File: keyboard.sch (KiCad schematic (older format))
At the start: 180 parts, among them SW1 SW_Push, U1 ATmega32U4-AU, Y1 16MHz

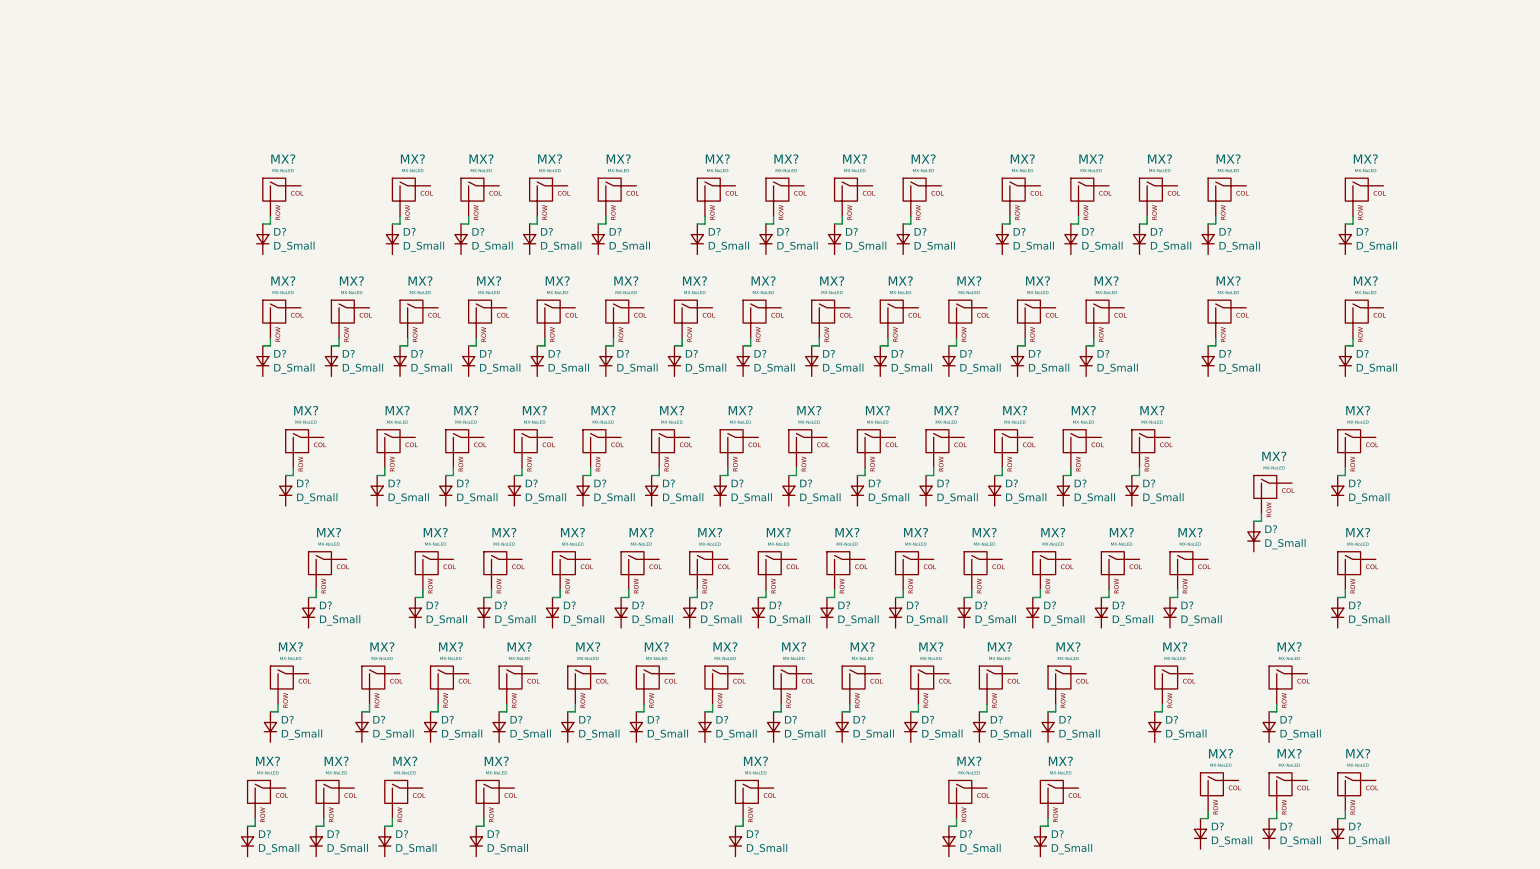
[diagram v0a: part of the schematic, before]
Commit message: Added labels for rows and columns
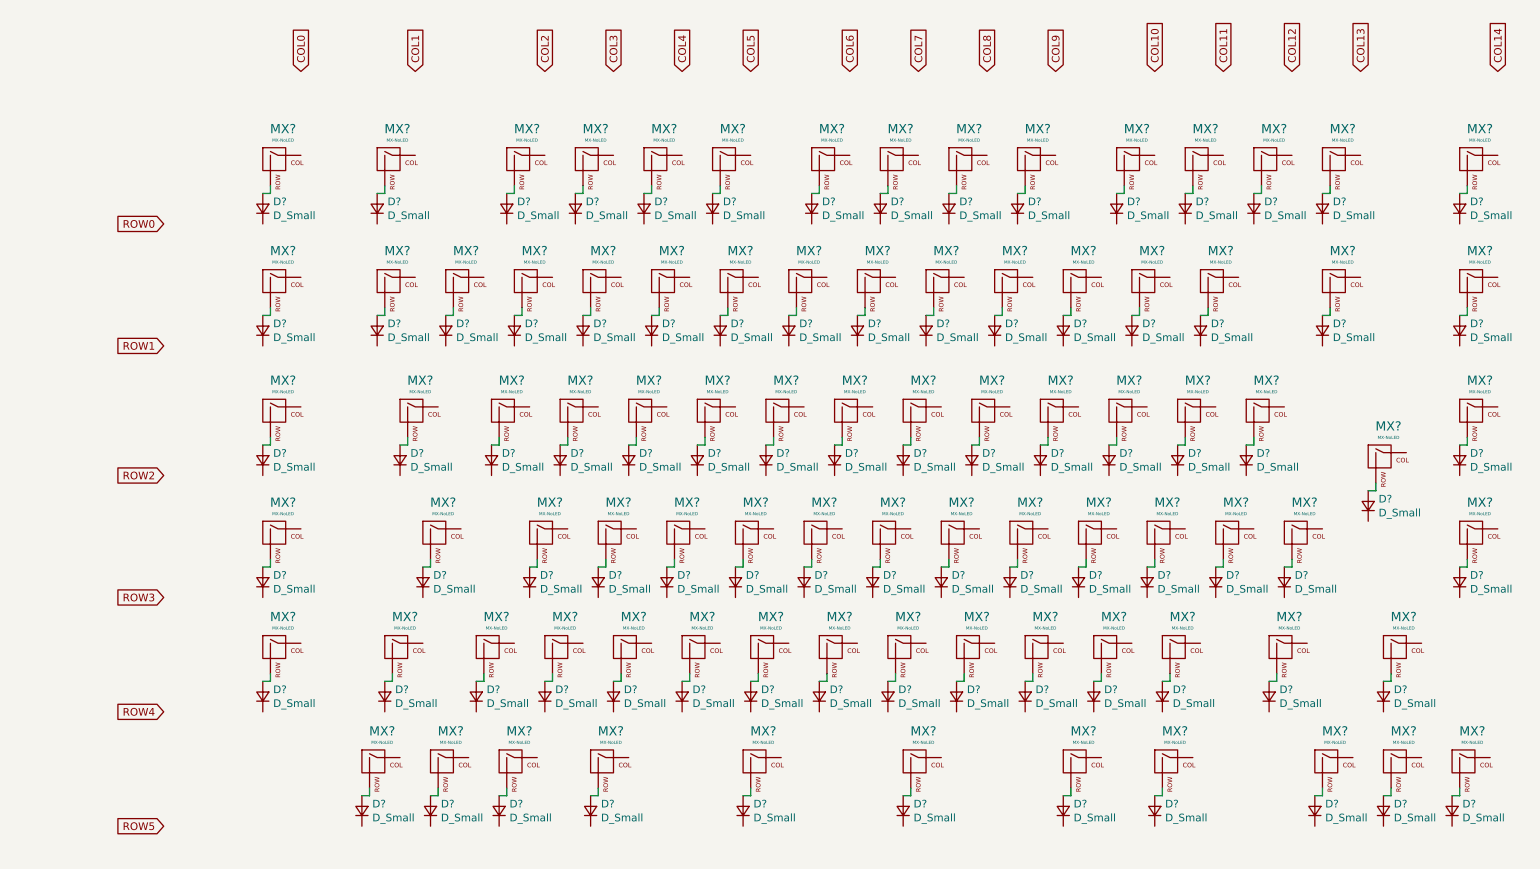
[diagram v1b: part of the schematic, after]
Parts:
- added D? (x6): D_Small, symbol Device:D_Small
- added MX? (x6): MX-NoLED, symbol MX_Alps_Hybrid:MX-NoLED
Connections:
- new net: D?.2 (A), MX?.2 (ROW) (x6)
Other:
- moved on the sheet: D?, MX?

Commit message: Key labeling
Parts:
- gave numbers to parts that had none: 88
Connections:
- net COL0: now also MX_XL1.1 (COL), MX_XL2.1 (COL), MX_XL3.1 (COL), MX_XL4.1 (COL), MX_XL5.1 (COL)
- net COL1: now also MX_BSLASH.1 (COL), MX_ESC.1 (COL), MX_FUNCTION.1 (COL), MX_LSHIFT.1 (COL)
- net COL2: now also MX_1.1 (COL), MX_CAPS.1 (COL), MX_CTRL.1 (COL), MX_TAB.1 (COL)
- net ROW0: now also D?.1 (K), D?.1 (K), D?.1 (K), D?.1 (K), D?.1 (K), D?.1 (K), D?.1 (K), D?.1 (K), D?.1 (K), D?.1 (K), D?.1 (K), D?.1 (K), D?.1 (K), D?.1 (K), D?.1 (K)
- net ROW1: now also D?.1 (K), D?.1 (K), D?.1 (K), D?.1 (K), D?.1 (K), D?.1 (K), D?.1 (K), D?.1 (K), D?.1 (K), D?.1 (K), D?.1 (K), D?.1 (K), D?.1 (K), D?.1 (K), D?.1 (K), D?.1 (K)
- net ROW2: now also D?.1 (K), D?.1 (K), D?.1 (K), D?.1 (K), D?.1 (K), D?.1 (K), D?.1 (K), D?.1 (K), D?.1 (K), D?.1 (K), D?.1 (K), D?.1 (K), D?.1 (K), D?.1 (K), D?.1 (K)
- net ROW3: now also D?.1 (K), D?.1 (K), D?.1 (K), D?.1 (K), D?.1 (K), D?.1 (K), D?.1 (K), D?.1 (K), D?.1 (K), D?.1 (K), D?.1 (K), D?.1 (K), D?.1 (K), D?.1 (K), D?.1 (K), D?.1 (K)
- net ROW4: now also D?.1 (K), D?.1 (K), D?.1 (K), D?.1 (K), D?.1 (K), D?.1 (K), D?.1 (K), D?.1 (K), D?.1 (K), D?.1 (K), D?.1 (K), D?.1 (K), D?.1 (K), D?.1 (K), D?.1 (K)
- net ROW5: now also D?.1 (K), D?.1 (K), D?.1 (K), D?.1 (K), D?.1 (K), D?.1 (K), D?.1 (K), D?.1 (K), D?.1 (K), D?.1 (K), D?.1 (K)

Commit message: Key wiring
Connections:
- net COL10: now also MX_9.1 (COL), MX_FN7.1 (COL), MX_I.1 (COL), MX_K.1 (COL), MX_M.1 (COL)
- net COL11: now also MXL.1 (COL), MX_0.1 (COL), MX_COMMA.1 (COL), MX_FN8.1 (COL), MX_O.1 (COL), MX_RCMD.1 (COL)
- net COL12: now also MX_ACC_O.1 (COL), MX_APOST.1 (COL), MX_DOT.1 (COL), MX_FN9.1 (COL), MX_P.1 (COL), MX_RALT.1 (COL)
- net COL13: now also MX_ACC_A.1 (COL), MX_ACC_E.1 (COL), MX_ACC_I.1 (COL), MX_DASH.1 (COL), MX_FN10.1 (COL)
- net COL14: now also MX_ACC_U.1 (COL), MX_FN11.1 (COL), MX_LEFT.1 (COL), MX_PLUS.1 (COL), MX_RSHIFT.1 (COL)
- net COL3: now also MX_2.1 (COL), MX_<.1 (COL), MX_A.1 (COL), MX_FN1.1 (COL), MX_LALT.1 (COL), MX_Q.1 (COL)
- net COL4: now also MX_3.1 (COL), MX_FN2.1 (COL), MX_LCMD.1 (COL), MX_S.1 (COL), MX_W.1 (COL), MX_Z.1 (COL)
- net COL5: now also MX_4.1 (COL), MX_D.1 (COL), MX_E.1 (COL), MX_FN3.1 (COL), MX_X.1 (COL)
- net COL6: now also MX_5.1 (COL), MX_C.1 (COL), MX_F.1 (COL), MX_FN4.1 (COL), MX_LSPACE.1 (COL), MX_R.1 (COL)
- net COL7: now also MX_6.1 (COL), MX_G.1 (COL), MX_T.1 (COL), MX_V.1 (COL)
- net COL8: now also MX_7.1 (COL), MX_B.1 (COL), MX_FN5.1 (COL), MX_H.1 (COL), MX_Y.1 (COL)
- net COL9: now also MX_8.1 (COL), MX_FN6.1 (COL), MX_J.1 (COL), MX_N.1 (COL), MX_RSPACE.1 (COL), MX_U.1 (COL)
- net COL15: now reaches MX_FN12.1 (COL)
- net COL15: now also MX_BSPACE.1 (COL), MX_DOWN.1 (COL), MX_ENTER.1 (COL), MX_UP.1 (COL)
- net COL16: now reaches MX_XR1.1 (COL)
- net COL16: now also MX_RIGHT.1 (COL), MX_XR2.1 (COL), MX_XR3.1 (COL), MX_XR4.1 (COL)

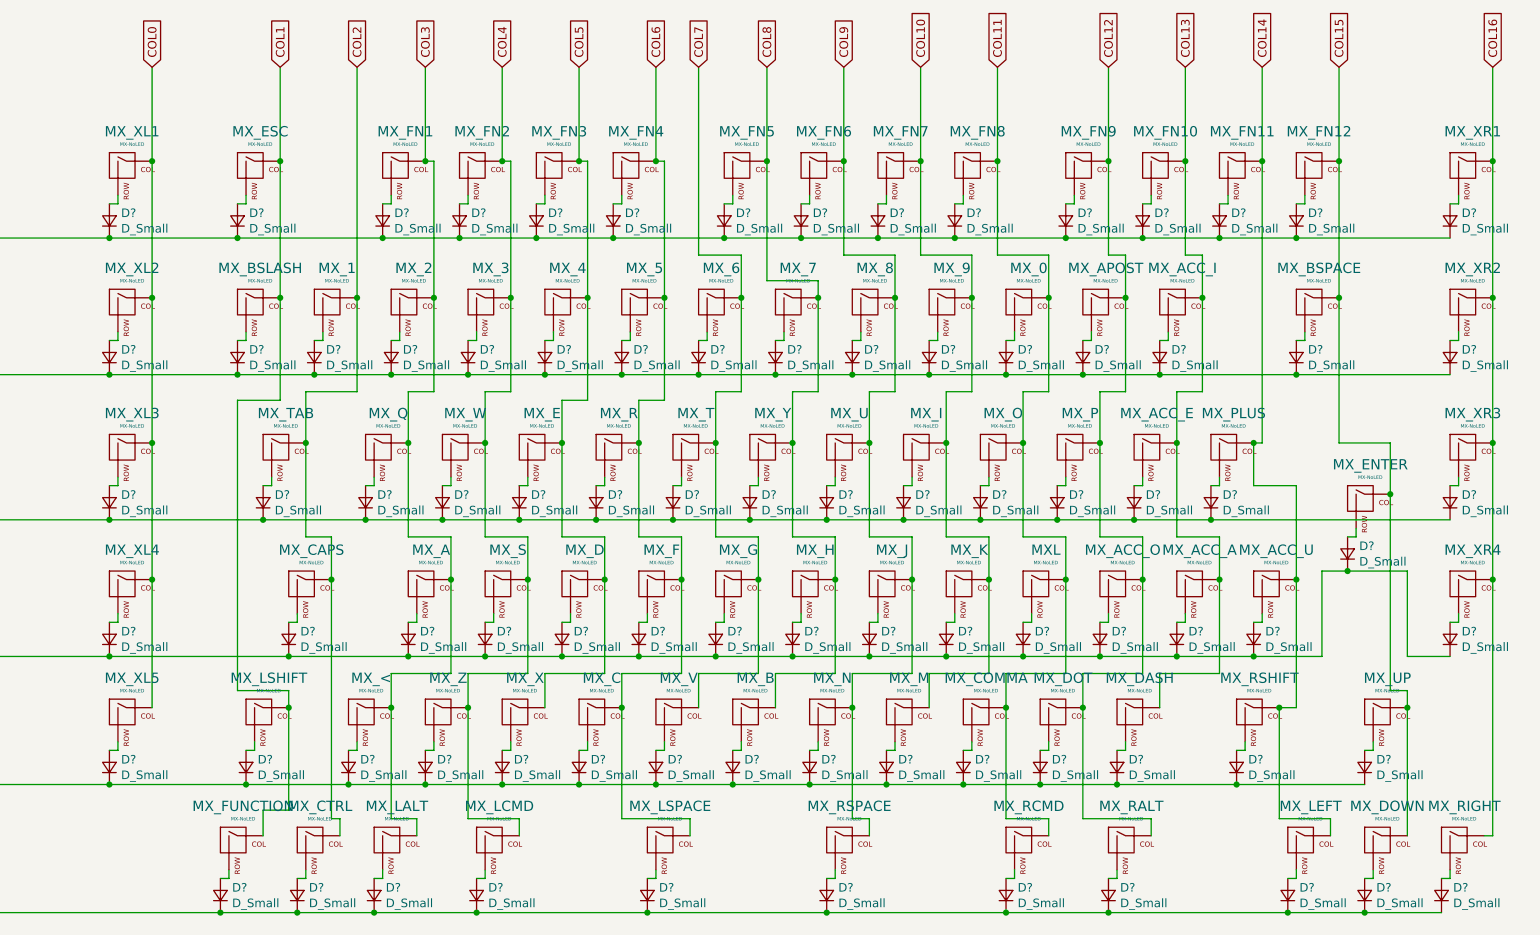
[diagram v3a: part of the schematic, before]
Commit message: Assigned all footprints except ENTER
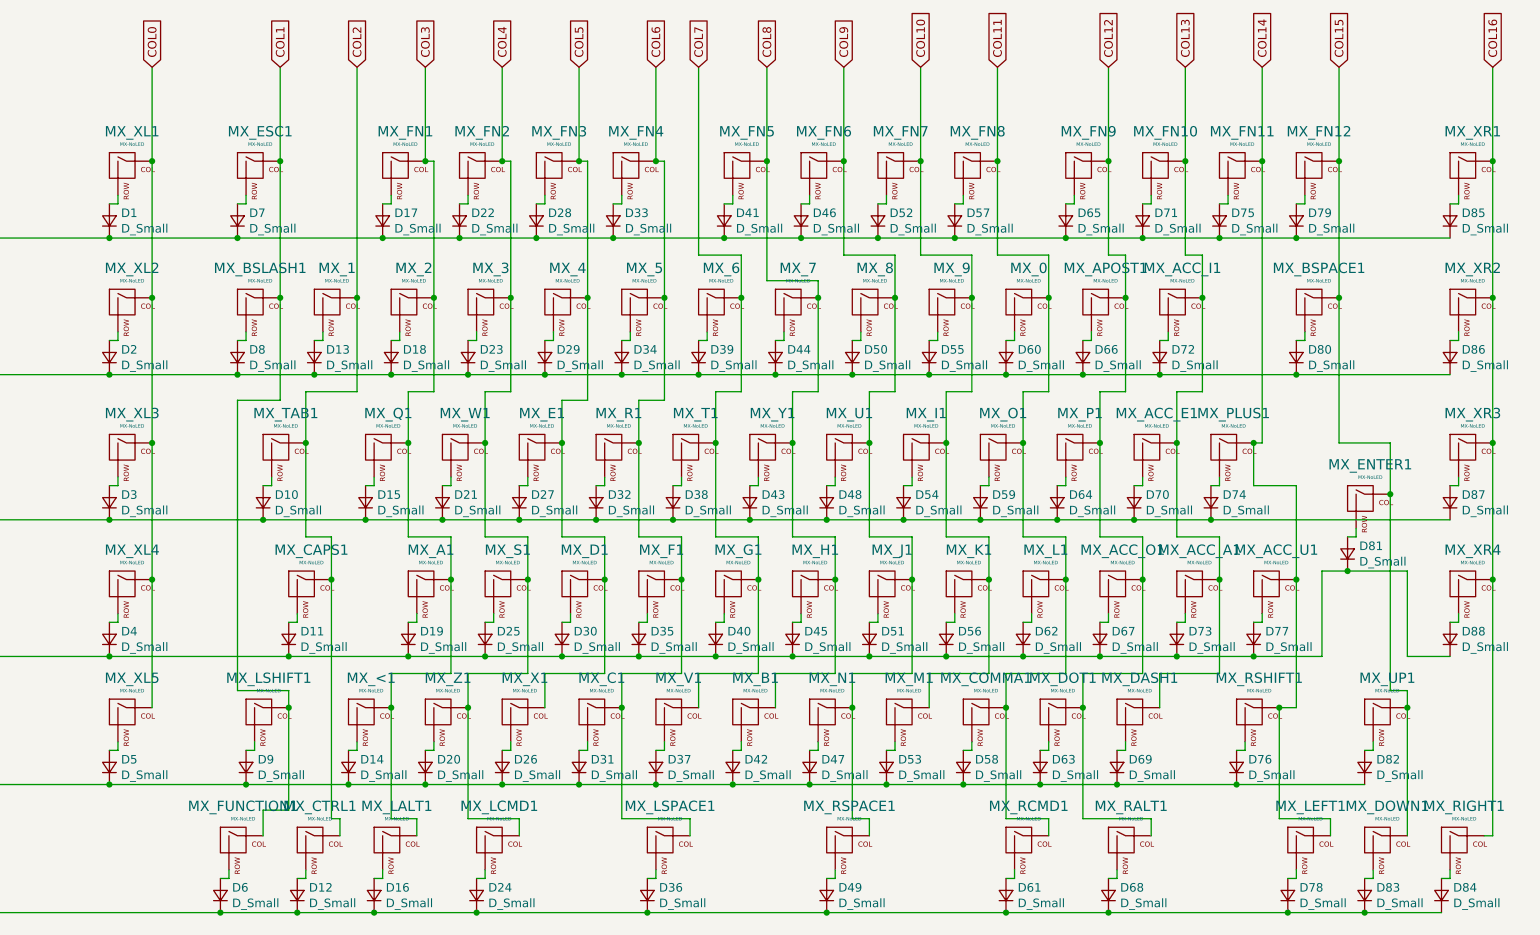
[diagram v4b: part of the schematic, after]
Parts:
- D1, D10, D11, D12, D13, D14, D15, D16, D17, D18, D19, D2, D20, D21, D22, D23, D24, D25, D26, D27, D28, D29, D3, D30, D31, D32, D33, D34, D35, D36, D37, D38, D39, D4, D40, D41, D42, D43, D44, D45, D46, D47, D48, D49, D5, D50, D51, D52, D53, D54, D55, D56, D57, D58, D59, D6, D60, D61, D62, D63, D64, D65, D66, D67, D68, D69, D7, D70, D71, D72, D73, D74, D75, D76, D77, D78, D79, D8, D80, D81, D82, D83, D84, D85, D86, D87, D88, D9: renamed from D?; footprint (none) -> Diode_SMD:D_SOD-123
- MX_0, MX_1, MX_2, MX_3, MX_4, MX_5, MX_6, MX_7, MX_8, MX_9, MX_FN1, MX_FN10, MX_FN11, MX_FN12, MX_FN2, MX_FN3, MX_FN4, MX_FN5, MX_FN6, MX_FN7, MX_FN8, MX_FN9, MX_XL1, MX_XL2, MX_XL3, MX_XL4, MX_XL5, MX_XR1, MX_XR2, MX_XR3, MX_XR4: footprint (none) -> MX_Alps_Hybrid:MX-1U-NoLED
- MX_<1: renamed from MX_<; footprint (none) -> MX_Alps_Hybrid:MX-1U-NoLED
- MX_A1: renamed from MX_A; footprint (none) -> MX_Alps_Hybrid:MX-1U-NoLED
- MX_ACC_A1: renamed from MX_ACC_A; footprint (none) -> MX_Alps_Hybrid:MX-1U-NoLED
- MX_ACC_E1: renamed from MX_ACC_E; footprint (none) -> MX_Alps_Hybrid:MX-1U-NoLED
- MX_ACC_I1: renamed from MX_ACC_I; footprint (none) -> MX_Alps_Hybrid:MX-1U-NoLED
- MX_ACC_O1: renamed from MX_ACC_O; footprint (none) -> MX_Alps_Hybrid:MX-1U-NoLED
- MX_ACC_U1: renamed from MX_ACC_U; footprint (none) -> MX_Alps_Hybrid:MX-1U-NoLED
- MX_APOST1: renamed from MX_APOST; footprint (none) -> MX_Alps_Hybrid:MX-1U-NoLED
- MX_B1: renamed from MX_B; footprint (none) -> MX_Alps_Hybrid:MX-1U-NoLED
- MX_BSLASH1: renamed from MX_BSLASH; footprint (none) -> MX_Alps_Hybrid:MX-1U-NoLED
- MX_BSPACE1: renamed from MX_BSPACE; footprint (none) -> MX_Alps_Hybrid:MX-2U-NoLED
- MX_C1: renamed from MX_C; footprint (none) -> MX_Alps_Hybrid:MX-1U-NoLED
- MX_CAPS1: renamed from MX_CAPS; footprint (none) -> MX_Alps_Hybrid:MX-1.75U-NoLED
- MX_COMMA1: renamed from MX_COMMA; footprint (none) -> MX_Alps_Hybrid:MX-1U-NoLED
- MX_CTRL1: renamed from MX_CTRL; footprint (none) -> MX_Alps_Hybrid:MX-1U-NoLED
- MX_D1: renamed from MX_D; footprint (none) -> MX_Alps_Hybrid:MX-1U-NoLED
- MX_DASH1: renamed from MX_DASH; footprint (none) -> MX_Alps_Hybrid:MX-1U-NoLED
- MX_DOT1: renamed from MX_DOT; footprint (none) -> MX_Alps_Hybrid:MX-1U-NoLED
- MX_DOWN1: renamed from MX_DOWN; footprint (none) -> MX_Alps_Hybrid:MX-1U-NoLED
- MX_E1: renamed from MX_E; footprint (none) -> MX_Alps_Hybrid:MX-1U-NoLED
- MX_ESC1: renamed from MX_ESC; footprint (none) -> MX_Alps_Hybrid:MX-1U-NoLED
- MX_F1: renamed from MX_F; footprint (none) -> MX_Alps_Hybrid:MX-1U-NoLED
- MX_FUNCTION1: renamed from MX_FUNCTION; footprint (none) -> MX_Alps_Hybrid:MX-1U-NoLED
- MX_G1: renamed from MX_G; footprint (none) -> MX_Alps_Hybrid:MX-1U-NoLED
- MX_H1: renamed from MX_H; footprint (none) -> MX_Alps_Hybrid:MX-1U-NoLED
- MX_I1: renamed from MX_I; footprint (none) -> MX_Alps_Hybrid:MX-1U-NoLED
- MX_J1: renamed from MX_J; footprint (none) -> MX_Alps_Hybrid:MX-1U-NoLED
- MX_K1: renamed from MX_K; footprint (none) -> MX_Alps_Hybrid:MX-1U-NoLED
- MX_L1: renamed from MXL; footprint (none) -> MX_Alps_Hybrid:MX-1U-NoLED
- MX_LALT1: renamed from MX_LALT; footprint (none) -> MX_Alps_Hybrid:MX-1U-NoLED
- MX_LCMD1: renamed from MX_LCMD; footprint (none) -> MX_Alps_Hybrid:MX-1.25U-NoLED
- MX_LEFT1: renamed from MX_LEFT; footprint (none) -> MX_Alps_Hybrid:MX-1U-NoLED
- MX_LSHIFT1: renamed from MX_LSHIFT; footprint (none) -> MX_Alps_Hybrid:MX-1.25U-NoLED
- MX_LSPACE1: renamed from MX_LSPACE; footprint (none) -> MX_Alps_Hybrid:MX-2.75U-NoLED
- MX_M1: renamed from MX_M; footprint (none) -> MX_Alps_Hybrid:MX-1U-NoLED
- MX_N1: renamed from MX_N; footprint (none) -> MX_Alps_Hybrid:MX-1U-NoLED
- MX_O1: renamed from MX_O; footprint (none) -> MX_Alps_Hybrid:MX-1U-NoLED
- MX_P1: renamed from MX_P; footprint (none) -> MX_Alps_Hybrid:MX-1U-NoLED
- MX_PLUS1: renamed from MX_PLUS; footprint (none) -> MX_Alps_Hybrid:MX-1U-NoLED
- MX_Q1: renamed from MX_Q; footprint (none) -> MX_Alps_Hybrid:MX-1U-NoLED
- MX_R1: renamed from MX_R; footprint (none) -> MX_Alps_Hybrid:MX-1U-NoLED
- MX_RALT1: renamed from MX_RALT; footprint (none) -> MX_Alps_Hybrid:MX-1U-NoLED
- MX_RCMD1: renamed from MX_RCMD; footprint (none) -> MX_Alps_Hybrid:MX-1.25U-NoLED
- MX_RIGHT1: renamed from MX_RIGHT; footprint (none) -> MX_Alps_Hybrid:MX-1U-NoLED
- MX_RSHIFT1: renamed from MX_RSHIFT; footprint (none) -> MX_Alps_Hybrid:MX-1.75U-NoLED
- MX_RSPACE1: renamed from MX_RSPACE; footprint (none) -> MX_Alps_Hybrid:MX-2.25U-NoLED
- MX_S1: renamed from MX_S; footprint (none) -> MX_Alps_Hybrid:MX-1U-NoLED
- MX_T1: renamed from MX_T; footprint (none) -> MX_Alps_Hybrid:MX-1U-NoLED
- MX_TAB1: renamed from MX_TAB; footprint (none) -> MX_Alps_Hybrid:MX-1.5U-NoLED
- MX_U1: renamed from MX_U; footprint (none) -> MX_Alps_Hybrid:MX-1U-NoLED
- MX_UP1: renamed from MX_UP; footprint (none) -> MX_Alps_Hybrid:MX-1U-NoLED
- MX_V1: renamed from MX_V; footprint (none) -> MX_Alps_Hybrid:MX-1U-NoLED
- MX_W1: renamed from MX_W; footprint (none) -> MX_Alps_Hybrid:MX-1U-NoLED
- MX_X1: renamed from MX_X; footprint (none) -> MX_Alps_Hybrid:MX-1U-NoLED
- MX_Y1: renamed from MX_Y; footprint (none) -> MX_Alps_Hybrid:MX-1U-NoLED
- MX_Z1: renamed from MX_Z; footprint (none) -> MX_Alps_Hybrid:MX-1U-NoLED
- SW1: footprint (none) -> random-keyboard-parts:SKQG-1155865
- USB1: footprint (none) -> random-keyboard-parts:Molex-0548190589
- renumbered MX_ENTER to MX_ENTER1

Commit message: Assigned ENTER footprints and started pcb
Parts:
- MX_ENTER1: footprint (none) -> MX_Alps_Hybrid:MX-ISO-ReversedStabilizers
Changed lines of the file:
@@
 F 0 "MX_ENTER1" H 20133 3973 60  0000 C CNN
 F 1 "MX-NoLED" H 20133 3899 20  0000 C CNN
-F 2 "" H 19475 3725 60  0001 C CNN
+F 2 "MX_Alps_Hybrid:MX-ISO-ReversedStabilizers" H 19475 3725 60  0001 C CNN
 F 3 "" H 19475 3725 60  0001 C CNN
 	1    20100 3750
